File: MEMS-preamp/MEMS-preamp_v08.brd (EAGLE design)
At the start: 51 x 30 mm, 45 parts, among them IC1 DMN2400, IC2 BQ21040, IC3 BQ297X, IC4 SC4503, IC5 TPS7A49, IC6 OPA2134, J2 Battery, SW1 SPDT

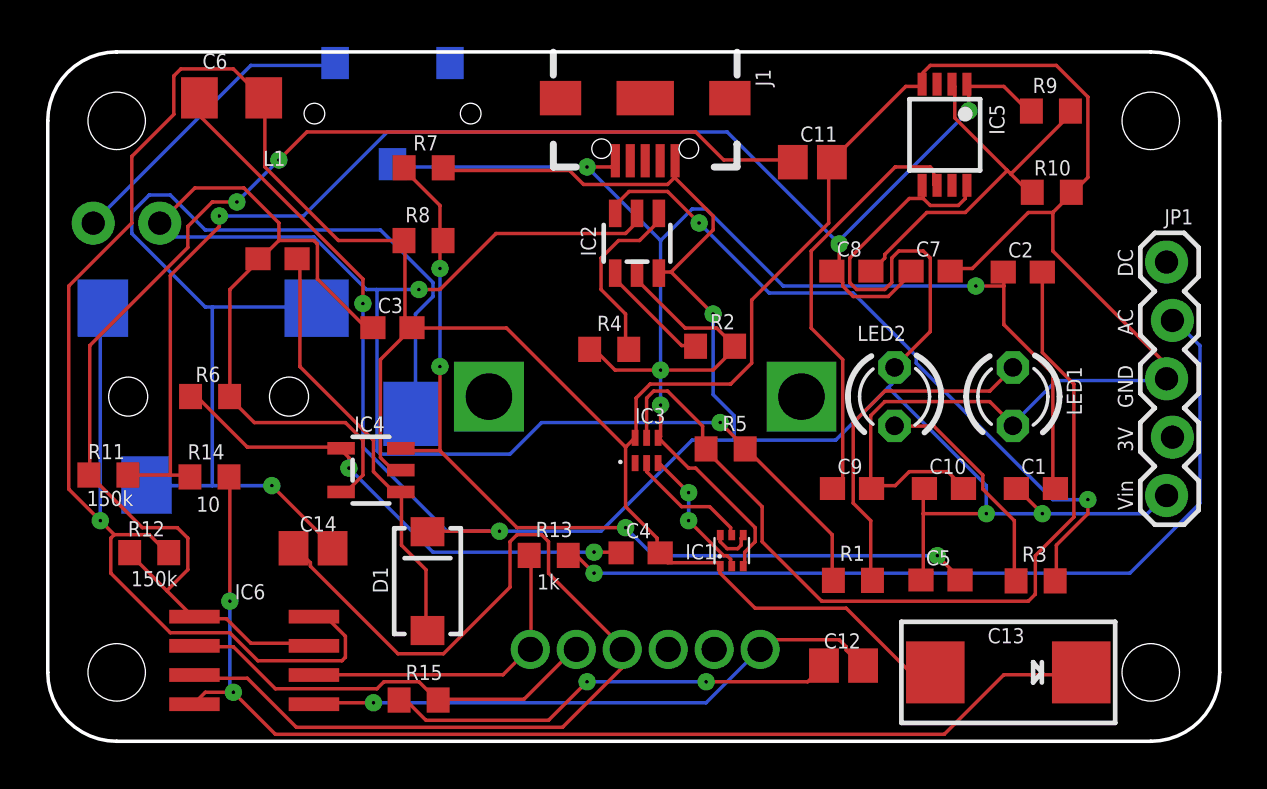
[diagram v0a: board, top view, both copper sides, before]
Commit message: Vin of ICS40300 changed back to 12V pin for now
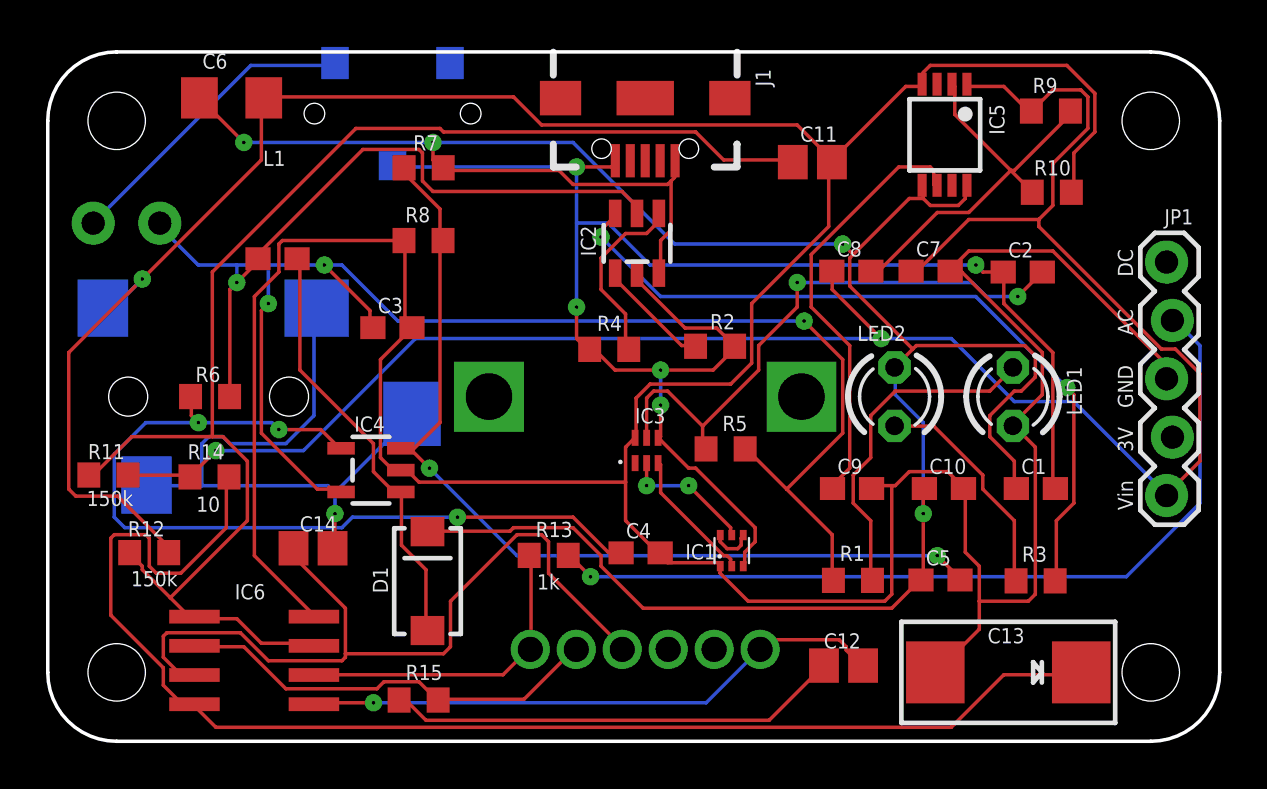
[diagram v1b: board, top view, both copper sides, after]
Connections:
- net +12V: now also JP1.1
- net V+: no longer JP1.1
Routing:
- net +12V: track 63.8 -> 89.2 mm, vias 3 -> 2
- net N$7: track 48.5 -> 27.8 mm
- net GND: track 183.0 -> 202.9 mm
- net N$13: track 21.8 -> 38.0 mm, vias 2 -> 3
- net N$18: track 39.4 -> 25.3 mm, vias 0 -> 2
- net N$10: track 44.0 -> 35.2 mm
- net V+: track 117.9 -> 109.4 mm, vias 5 -> 4
- net N$1: track 50.2 -> 58.7 mm, vias 2 -> 0
- net VBAT: track 86.1 -> 89.8 mm, vias 2 -> 4
- net N$15: track 31.1 -> 33.1 mm
- net N$8: track 59.1 -> 61.0 mm, vias 2 -> 0
- net N$14: track 39.9 -> 41.0 mm, vias 4 -> 2
- net GND2: track 71.0 -> 71.6 mm, vias 4 -> 5
- net N$20: track 5.40 -> 5.75 mm, vias 0 -> 2
- net N$4: vias 2 -> 0
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
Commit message: Add files via upload
Changes made to MEMS board V08
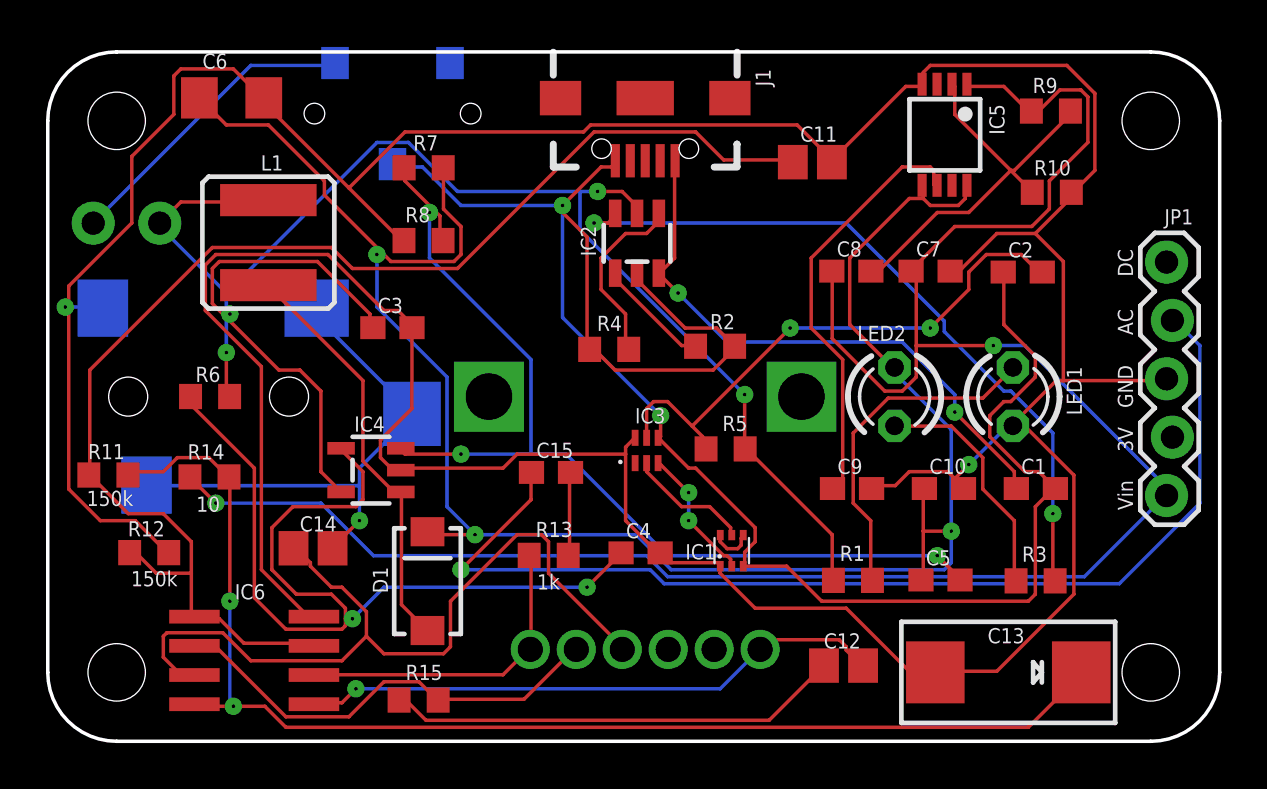
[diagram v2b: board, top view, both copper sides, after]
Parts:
- added C15: 10uF, rcl:C0603
- L1: device SparkFun-Passives:0603 -> SparkFun-Passives:CR54
- moved L1 0.81 mm to (9.60, 21.7)
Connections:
- net GROU[ renamed N$21
- new net N$23: C15.2, R13.1
- new net VUSB: C1.1, IC2.6, J1.VBUS
- net +12V: no longer R11.2
- net N$1: now also R11.2
- net N$12: now also L1.P$2; no longer L1.2
- net N$3: now also C15.1; no longer R13.1
- net V+: no longer C1.1, IC2.6, J1.VBUS
- net VBAT: now also L1.P$1; no longer L1.1
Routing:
- net VUSB: track 0.00 -> 25.5 mm, vias 0 -> 2
- net V+: track 109.4 -> 84.7 mm, vias 4 -> 3
- net VBAT: track 89.8 -> 79.0 mm
- net N$3: track 37.7 -> 47.9 mm
- net GND2: track 71.6 -> 81.7 mm, vias 5 -> 2
- net GND: track 202.9 -> 194.6 mm, vias 1 -> 2
- net N$7: track 27.8 -> 22.8 mm
- net N$23: track 0.00 -> 3.63 mm
- net N$1: track 58.7 -> 55.3 mm, vias 0 -> 2
- net N$13: track 38.0 -> 41.3 mm, vias 3 -> 2
- net N$8: track 61.0 -> 58.7 mm
- net N$14: track 41.0 -> 43.3 mm, vias 2 -> 3
- net +12V: track 89.2 -> 91.0 mm
- net N$15: track 33.1 -> 31.7 mm
- net N$18: track 25.3 -> 24.2 mm
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
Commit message: Add files via upload
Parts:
- removed IC2: BQ21040, CMU-ArtFab:SOT23-6
- removed IC3: BQ297X, CMU-ArtFab:WSON-6
- removed J1: (no value), SparkFun-Connectors:USB-B-MICRO-SMD_RED_PASTE
- removed J2: Battery, SparkFun-Connectors:1X02_LOCK
- removed R5: 330, CMU-ArtFab:R0603
- removed SW1: SPDT, CMU-ArtFab:SWITCH_SPDT_CL-SB-12B
- added C16: 4.7uF, rcl:C0603
- added J4: (no value), CMU-ArtFab:USB-B-MICRO-SMD_RED_PASTE
- added J5: Battery, SparkFun-Connectors:1X02_LOCK
- added R16: 330, CMU-ArtFab:R0603
- added R22, R23: 10M, CMU-ArtFab:R0603
- added SW3: SPDT, CMU-ArtFab:SWITCH_SPDT_CL-SB-12B
- added U$1: MCP73831, CMU-ArtFab:SOT-23-5
- added U$2: QS6K1, CMU-ArtFab:SOT457R_PHILIPS
- C1: value 10uF -> 4.7uF
- IC1: value DMN2400 -> BQ297X; device CMU-ArtFab:SOT-563 -> CMU-ArtFab:WSON-6-LONG
- IC6: value OPA2134 -> TL072D
- LED2: value (none) -> Charge
- R2: value 10k -> 470
- R3: value 1k -> 5k
- R4: value 10k -> 2.2k
- moved C5 22.9 mm to (16.2, 3.12)
- moved C12 22.6 mm to (12.2, 6.09)
- moved R3 21.4 mm to (39.1, 28.0)
- moved R4 20.2 mm to (43.5, 10.4)
- moved IC6 19.8 mm to (23.9, 16.6), turned to 0 degrees
- moved C13 19.5 mm to (23.0, 8.10)
- moved R9 18.3 mm to (25.9, 23.0)
- moved C11 18.0 mm to (15.6, 22.2)
- moved IC1 17.7 mm to (38.8, 23.5)
- moved C1 17.3 mm to (28.2, 19.9)
- moved IC5 17.1 mm to (22.0, 24.2)
- moved R1 16.0 mm to (19.9, 1.70)
- moved R10 13.6 mm to (30.1, 23.0)
- moved C15 13.1 mm to (34.3, 7.50)
- moved R8 12.4 mm to (11.8, 10.3)
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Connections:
- removed net GND2: C1.2, C2.1, IC1.3, IC2.5, IC3.4, J1.GND, R2.1, R4.1, SW1.P$2
- removed net N$15: IC2.3, R3.2
- removed net N$16: IC2.1, R4.2
- removed net N$17: IC2.4, R2.2
- removed net N$18: C2.2, IC3.5, R5.2
- removed net N$19: IC1.4, IC1.6
- removed net N$20: IC1.5, IC3.2
- removed net VUSB: C1.1, IC2.6, J1.VBUS
- new net +5V: C1.1, J4.VBUS, LED2.A, U$1.4
- new net BATGND: C2.1, IC1.4, SW3.P$2, U$2.6
- new net N$25: R2.2, U$1.1
- new net N$27: IC1.3, R23.2, U$2.1
- new net N$31: IC1.2, R22.2, U$2.3
- new net N$34: IC1.6, R4.2
- new net N$42: C2.2, IC1.5, R16.2
- new net USBGND: C1.2, C16.2, J4.GND, J5.2, R3.1, SW3.P$1, U$1.2
- net GND: now also R22.1, R23.1, R4.1, U$2.2; no longer IC1.1, IC3.6
- net N$10: now also IC6.1; no longer IC6.7
- net N$11: now also U$2.4, U$2.5; no longer LED2.K, R3.1
- net N$21: now also IC6.2; no longer IC6.6
- net N$22: now also LED2.K, R2.1; no longer IC1.2, IC3.3
- net N$5: now also IC6.6; no longer IC6.2
- net N$6: now also R3.2, U$1.5; no longer J2.2, SW1.P$1
- net N$9: now also IC6.7; no longer IC6.1
- net V+: no longer LED2.A
- net VBAT: now also C16.1, J5.1, R16.1, U$1.3; no longer IC2.2, J2.1, R5.1
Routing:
- net GND2: track 81.7 -> 0.00 mm, vias 2 -> 0
- net USBGND: track 0.00 -> 59.8 mm, vias 0 -> 3
- net VBAT: track 79.0 -> 135.6 mm, vias 4 -> 5
- net BATGND: track 0.00 -> 40.6 mm, vias 0 -> 1
- net GND: track 194.6 -> 231.0 mm, vias 2 -> 4
- net N$2: track 14.9 -> 49.8 mm
- net N$15: track 31.7 -> 0.00 mm, vias 2 -> 0
- net V+: track 84.7 -> 56.2 mm, vias 3 -> 5
- net N$42: track 0.00 -> 27.8 mm
- net +5V: track 0.00 -> 27.4 mm, vias 0 -> 2
- net VUSB: track 25.5 -> 0.00 mm, vias 2 -> 0
- net N$18: track 24.2 -> 0.00 mm, vias 2 -> 0
- net N$9: track 25.6 -> 48.9 mm, vias 1 -> 4
- net N$3: track 47.9 -> 24.7 mm, vias 1 -> 0
- net N$5: track 14.0 -> 31.4 mm, vias 0 -> 3
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
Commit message: Add files via upload
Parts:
- removed C13: 100uF, microbuilder:EIA7343-31/D-R
- removed IC6: TL072D, linear:SO08
- removed R14: 10, CMU-ArtFab:R0603
- added C17: 0.1uF, adafruit:C0805K
- added IC2: OPA2134UA, linear:SO08
- added L2: 100uH/500mA, rcl:L3225M
- C15: device rcl:C0603 -> rcl:C1206
- moved C15 0.58 mm to (34.6, 7.00), turned to 180 degrees
- moved R16 0.50 mm to (39.4, 6.70)
- moved D1 0.41 mm to (16.5, 7.67), turned to 270 degrees
- moved R7 0.22 mm to (12.1, 24.1), turned to 180 degrees
- moved C11 0.22 mm to (15.8, 22.1)
- moved C5 0.22 mm to (16.4, 3.02), turned to 180 degrees
- moved C7 0.20 mm to (38.7, 10.3)
- moved IC1 0.20 mm to (39.0, 23.5)
- moved R22 0.20 mm to (39.0, 18.7)
- moved R3 0.20 mm to (39.1, 28.2), turned to 180 degrees
- moved C14 0.14 mm to (7.14, 8.30), turned to 180 degrees
- moved R4 0.14 mm to (43.4, 10.3)
- moved R10 0.14 mm to (30.0, 23.1)
- moved U$2 0.14 mm to (42.8, 23.1)
- moved C1 0.10 mm to (28.2, 20.0)
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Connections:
- removed net N$1: C13.+, IC6.8, R11.2, R14.1
- new net N$15: C17.1, IC2.8, L2.2, R11.2
- net +12V: now also L2.1; no longer R14.2
- net GND: now also C17.2, IC2.4; no longer C13.-, IC6.4
- net N$10: now also IC2.7; no longer IC6.1
- net N$21: now also IC2.6; no longer IC6.2
- net N$5: now also IC2.2; no longer IC6.6
- net N$8: now also IC2.3, IC2.5; no longer IC6.3, IC6.5
- net N$9: now also IC2.1; no longer IC6.7
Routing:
- net N$1: track 61.6 -> 0.00 mm, vias 6 -> 0
- net N$15: track 0.00 -> 55.3 mm, vias 0 -> 3
- net GND: track 231.0 -> 199.7 mm, vias 4 -> 5
- net USBGND: track 59.8 -> 82.8 mm, vias 3 -> 0
- net N$2: track 49.8 -> 29.3 mm
- net +12V: track 87.6 -> 67.8 mm
- net N$10: track 30.8 -> 48.1 mm, vias 2 -> 1
- net VBAT: track 135.6 -> 118.5 mm
- net N$9: track 48.9 -> 35.1 mm, vias 4 -> 3
- net N$14: track 58.6 -> 45.0 mm, vias 0 -> 2
- net N$8: track 54.5 -> 42.0 mm, vias 0 -> 2
- net N$34: track 17.3 -> 28.3 mm
- net V+: track 56.2 -> 66.2 mm, vias 5 -> 4
- net N$5: track 31.4 -> 21.6 mm, vias 3 -> 0
- net N$42: track 27.8 -> 37.1 mm, vias 0 -> 2
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
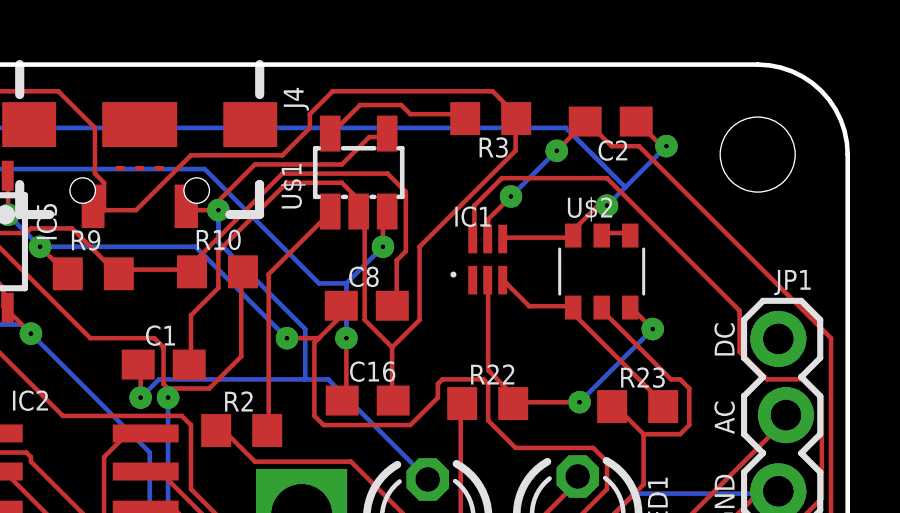
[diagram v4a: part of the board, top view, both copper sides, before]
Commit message: Add files via upload
IC names changed according to convention
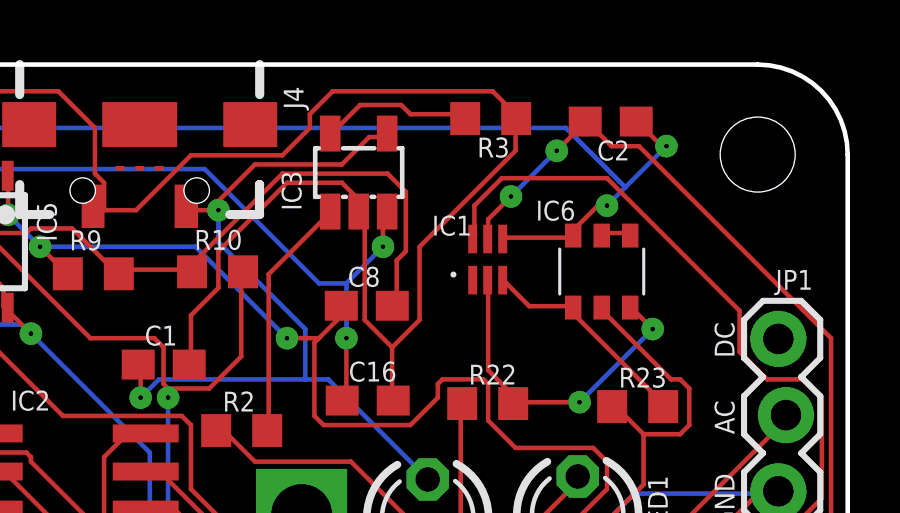
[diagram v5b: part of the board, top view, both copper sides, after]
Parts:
- renumbered U$1 to IC3, U$2 to IC6
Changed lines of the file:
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@@
 </element>
 <element name="IC1" library="CMU-ArtFab" package="WSON-6-LONG" value="BQ297X" x="39" y="23.5" smashed="yes">
-<attribute name="NAME" x="37.84" y="24.6" size="0.6604" layer="25" font="vector" ratio="15"/>
+<attribute name="NAME" x="37.14" y="24.3" size="0.6604" layer="25" font="vector" ratio="15"/>
 <attribute name="VALUE" x="38.24" y="22.222" size="0.6604" layer="27" font="vector" ratio="15" align="top-left"/>
 </element>
@@
 <attribute name="VALUE" x="43.635" y="29.605" size="0.6604" layer="27" font="vector" ratio="15" rot="R180"/>
 </element>
-<element name="U$1" library="CMU-ArtFab" package="SOT-23-5" value="MCP73831" x="34.7" y="26.4" smashed="yes">
+<element name="IC3" library="CMU-ArtFab" package="SOT-23-5" value="MCP73831" x="34.7" y="26.4" smashed="yes">
 <attribute name="NAME" x="32.795" y="25.13" size="0.6604" layer="25" font="vector" ratio="15" rot="R90"/>
 <attribute name="VALUE" x="37.24" y="25.13" size="0.6604" layer="27" font="vector" ratio="15" rot="R90"/>
 </element>
-<element name="U$2" library="CMU-ArtFab" package="SOT457R_PHILIPS" value="QS6K1" x="42.8" y="23.1" smashed="yes">
-<attribute name="NAME" x="41.6" y="24.9" size="0.6604" layer="25" font="vector" ratio="15"/>
-<attribute name="VALUE" x="41.6" y="20" size="0.6604" layer="27" font="vector" ratio="15"/>
+<element name="IC6" library="CMU-ArtFab" package="SOT457R_PHILIPS" value="QS6K1" x="42.8" y="23.1" smashed="yes">
+<attribute name="NAME" x="40.6" y="24.8" size="0.6604" layer="25" font="vector" ratio="15"/>
+<attribute name="VALUE" x="41.5" y="20.6" size="0.6604" layer="27" font="vector" ratio="15"/>
 </element>
 <element name="R4" library="CMU-ArtFab" package="R0603" value="2.2k" x="43.4" y="10.3" smashed="yes">
@@
 <contactref element="C7" pad="2"/>
 <contactref element="IC4" pad="2"/>
-<contactref element="U$2" pad="2"/>
+<contactref element="IC6" pad="2"/>
 <contactref element="R22" pad="1"/>
 <contactref element="R23" pad="1"/>
@@
 <contactref element="J5" pad="1"/>
 <contactref element="R16" pad="1"/>
-<contactref element="U$1" pad="3"/>
+<contactref element="IC3" pad="3"/>
 <contactref element="C16" pad="1"/>
 <wire x1="7.3152" y1="1.6764" x2="19.05" y2="1.6764" width="0.1524" layer="1"/>
@@
 <contactref element="IC1" pad="4"/>
 <contactref element="C2" pad="1"/>
-<contactref element="U$2" pad="6"/>
+<contactref element="IC6" pad="6"/>
 <wire x1="39.624" y1="24.2316" x2="41.7576" y2="24.2316" width="0.1524" layer="1"/>
 <wire x1="41.7576" y1="24.2316" x2="41.85" y2="24.3" width="0.1524" layer="1"/>
@@
 </signal>
 <signal name="N$6">
-<contactref element="U$1" pad="5"/>
+<contactref element="IC3" pad="5"/>
 <contactref element="R3" pad="2"/>
 <wire x1="36.4236" y1="28.3464" x2="38.1" y2="28.3464" width="0.1524" layer="1"/>
@@
 <signal name="N$25">
 <contactref element="R2" pad="2"/>
-<contactref element="U$1" pad="1"/>
+<contactref element="IC3" pad="1"/>
 <wire x1="31.6992" y1="23.0124" x2="31.6992" y2="17.8308" width="0.1524" layer="1"/>
 <wire x1="33.6804" y1="24.9936" x2="31.6992" y2="23.0124" width="0.1524" layer="1"/>
@@
 </signal>
 <signal name="N$11">
-<contactref element="U$2" pad="5"/>
-<contactref element="U$2" pad="4"/>
+<contactref element="IC6" pad="5"/>
+<contactref element="IC6" pad="4"/>
 <wire x1="43.7388" y1="24.384" x2="42.8244" y2="24.384" width="0.1524" layer="1"/>
 <wire x1="42.8244" y1="24.384" x2="42.8" y2="24.3" width="0.1524" layer="1"/>
@@
 </signal>
 <signal name="N$27">
-<contactref element="U$2" pad="1"/>
+<contactref element="IC6" pad="1"/>
 <contactref element="IC1" pad="3"/>
 <contactref element="R23" pad="2"/>
@@
 </signal>
 <signal name="N$31">
-<contactref element="U$2" pad="3"/>
+<contactref element="IC6" pad="3"/>
 <contactref element="IC1" pad="2"/>
 <contactref element="R22" pad="2"/>
@@
 <contactref element="C1" pad="2"/>
 <contactref element="C16" pad="2"/>
-<contactref element="U$1" pad="2"/>
+<contactref element="IC3" pad="2"/>
 <contactref element="SW3" pad="P$1"/>
 <contactref element="J5" pad="2"/>
@@
 <contactref element="J4" pad="VBUS"/>
 <contactref element="C1" pad="1"/>
-<contactref element="U$1" pad="4"/>
+<contactref element="IC3" pad="4"/>
 <contactref element="LED2" pad="A"/>
 <wire x1="35.052" y1="27.5844" x2="35.5092" y2="27.5844" width="0.1524" layer="1"/>
